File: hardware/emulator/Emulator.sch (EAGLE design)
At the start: 41 parts, among them T1 ZVP2106ASTZ, T2 2N5401, U1 DEV-16771_REDUCED_PINS, U2 OPA2277PA, U3 MCP4822-E/P, U4 LM6132BIN, U5 L7808ABV, U6 L7908CV

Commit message: Update info text
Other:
- note added: "Maximum Emulation Current: 4.095 / R_Range Example: 4.095 / 49.9 = 0.082064 A = 82.06 mA"
- note added: "V_OC = 2 * DAC_OC_VOLTAGE_EMULATION"
- note removed: "Maximum Emulation Current: 3.3 / R_Range Example: 3.3 / 49.9 = 0.0661322 A = 66.13 mA"
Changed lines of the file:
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@@
 <wire x1="144.78" y1="132.08" x2="96.52" y2="132.08" width="0.508" layer="97" style="longdash"/>
 <text x="109.22" y="134.62" size="1.778" layer="97">Solar Cell Model</text>
-<text x="73.66" y="157.48" size="1.778" layer="97">Maximum Emulation Current: 3.3 / R_Range
-Example: 3.3 / 49.9 = 0.0661322 A = 66.13 mA</text>
+<text x="73.66" y="157.48" size="1.778" layer="97">Maximum Emulation Current: 4.095 / R_Range
+Example: 4.095 / 49.9 = 0.082064 A = 82.06 mA</text>
 <text x="50.8" y="121.92" size="1.778" layer="97">I_OUT = DAC_SC / R_RANGE</text>
+<text x="149.86" y="73.66" size="1.778" layer="97" rot="R90">V_OC = 2 * DAC_OC_VOLTAGE_EMULATION</text>
 </plain>
 <instances>

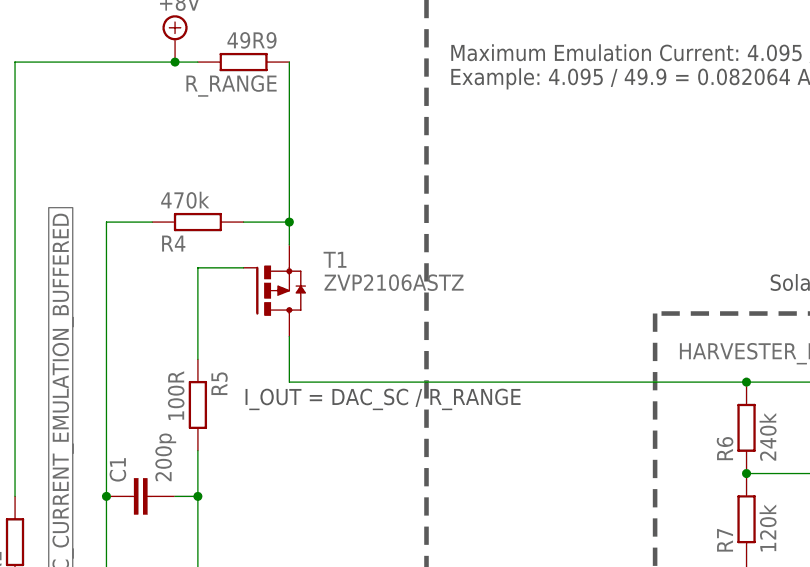
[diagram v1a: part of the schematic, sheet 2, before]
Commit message: Update the emulation MOSFET device
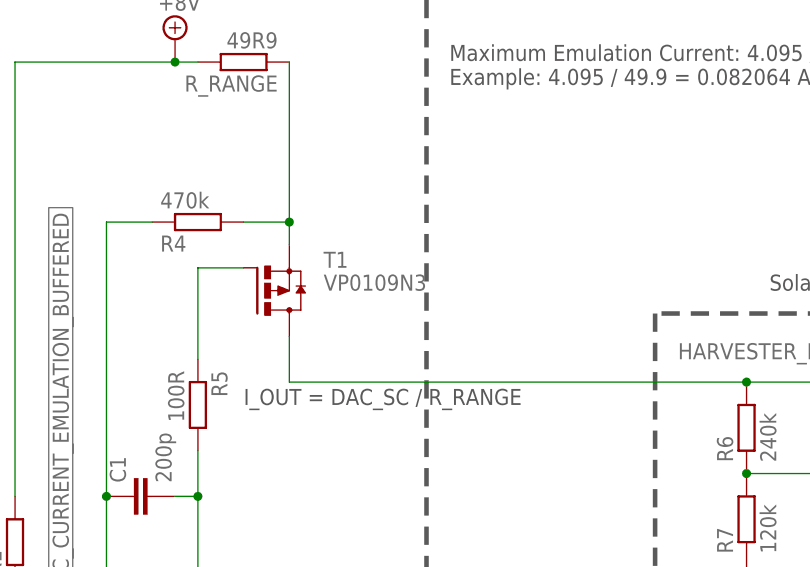
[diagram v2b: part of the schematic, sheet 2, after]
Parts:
- T1: value ZVP2106ASTZ -> VP0109N3; device ZVP2106A:ZVP2106ASTZ -> ZVP2106A:VP0109N3
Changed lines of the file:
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@@
 <part name="SUPPLY8" library="supply2" library_urn="urn:adsk.eagle:library:372" deviceset="GND" device=""/>
 <part name="SUPPLY18" library="supply2" library_urn="urn:adsk.eagle:library:372" deviceset="+8V" device=""/>
-<part name="T1" library="ZVP2106A" deviceset="ZVP2106ASTZ" device=""/>
+<part name="T1" library="ZVP2106A" deviceset="VP0109N3" device=""/>
 <part name="T2" library="transistor-neu-to92" deviceset="*-PNP-" device="TO92-EBC" package3d_urn="urn:adsk.eagle:package:28763/2" technology="2N5401" value="2N5401"/>
 <part name="R7" library="rcl" library_urn="urn:adsk.eagle:library:334" deviceset="R-EU_" device="0207/10" package3d_urn="urn:adsk.eagle:package:23491/2" value="120k"/>

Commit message: Update board version
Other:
- note added: "v0.3.11"
- note removed: "v0.2.3"
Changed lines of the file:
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@@
 <plain>
 <text x="215.9" y="20.32" size="2.54" layer="94">SOCRAETES Emulator</text>
-<text x="215.9" y="15.24" size="2.54" layer="94">v0.2.3</text>
+<text x="215.9" y="15.24" size="2.54" layer="94">v0.3.11</text>
 <text x="215.9" y="10.16" size="2.54" layer="94">Author: S.Mosavat</text>
 <text x="162.56" y="7.62" size="2.54" layer="94">University of Duisburg-Essen

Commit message: Add minor changes to the hardware
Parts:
- added T3: 2N5401, transistor-neu-to92:2N5401-PNP-TO92-EBC
- R1, R2: value 1k5 -> 1k
- R3, R4: value 470k -> 499k
- T2: value 2N5401 -> IRF9530PBF; device transistor-neu-to92:2N5401-PNP-TO92-EBC -> IRF9530PBF:IRF9530PBF
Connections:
- net GND: now also T3.C; no longer T2.C
- net HARVESTER_EMULATION: now also T2.D, T3.E; no longer T2.E
- net N$12: now also T3.B; no longer T2.B
- net N$5: now also T2.G
- net N$7: now also T2.S
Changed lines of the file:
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@@
 <part name="SUPPLY17" library="supply2" library_urn="urn:adsk.eagle:library:372" deviceset="-8V" device=""/>
 <part name="U2" library="OPA2277PA" deviceset="OPA2277PA" device=""/>
-<part name="R1" library="rcl" library_urn="urn:adsk.eagle:library:334" deviceset="R-EU_" device="0207/10" package3d_urn="urn:adsk.eagle:package:23491/2" value="1k5"/>
-<part name="R2" library="rcl" library_urn="urn:adsk.eagle:library:334" deviceset="R-EU_" device="0207/10" package3d_urn="urn:adsk.eagle:package:23491/2" value="1k5"/>
-<part name="R3" library="rcl" library_urn="urn:adsk.eagle:library:334" deviceset="R-EU_" device="0207/10" package3d_urn="urn:adsk.eagle:package:23491/2" value="470k"/>
-<part name="R4" library="rcl" library_urn="urn:adsk.eagle:library:334" deviceset="R-EU_" device="0207/10" package3d_urn="urn:adsk.eagle:package:23491/2" value="470k"/>
+<part name="R1" library="rcl" library_urn="urn:adsk.eagle:library:334" deviceset="R-EU_" device="0207/10" package3d_urn="urn:adsk.eagle:package:23491/2" value="1k"/>
+<part name="R2" library="rcl" library_urn="urn:adsk.eagle:library:334" deviceset="R-EU_" device="0207/10" package3d_urn="urn:adsk.eagle:package:23491/2" value="1k"/>
+<part name="R3" library="rcl" library_urn="urn:adsk.eagle:library:334" deviceset="R-EU_" device="0207/10" package3d_urn="urn:adsk.eagle:package:23491/2" value="499k"/>
+<part name="R4" library="rcl" library_urn="urn:adsk.eagle:library:334" deviceset="R-EU_" device="0207/10" package3d_urn="urn:adsk.eagle:package:23491/2" value="499k"/>
 <part name="R_RANGE" library="rcl" library_urn="urn:adsk.eagle:library:334" deviceset="R-EU_" device="0207/10" package3d_urn="urn:adsk.eagle:package:23491/2" value="49R9"/>
 <part name="R5" library="rcl" library_urn="urn:adsk.eagle:library:334" deviceset="R-EU_" device="0207/10" package3d_urn="urn:adsk.eagle:package:23491/2" value="100R"/>
@@
 <part name="SUPPLY18" library="supply2" library_urn="urn:adsk.eagle:library:372" deviceset="+8V" device=""/>
 <part name="T1" library="ZVP2106A" deviceset="VP0109N3" device=""/>
-<part name="T2" library="transistor-neu-to92" deviceset="*-PNP-" device="TO92-EBC" package3d_urn="urn:adsk.eagle:package:28763/2" technology="2N5401" value="2N5401"/>
+<part name="T3" library="transistor-neu-to92" deviceset="*-PNP-" device="TO92-EBC" package3d_urn="urn:adsk.eagle:package:28763/2" technology="2N5401" value="2N5401"/>
 <part name="R7" library="rcl" library_urn="urn:adsk.eagle:library:334" deviceset="R-EU_" device="0207/10" package3d_urn="urn:adsk.eagle:package:23491/2" value="120k"/>
 <part name="R6" library="rcl" library_urn="urn:adsk.eagle:library:334" deviceset="R-EU_" device="0207/10" package3d_urn="urn:adsk.eagle:package:23491/2" value="240k"/>
@@
 <part name="R11" library="rcl" library_urn="urn:adsk.eagle:library:334" deviceset="R-EU_" device="0207/10" package3d_urn="urn:adsk.eagle:package:23491/2" value="330R"/>
 <part name="ERROR" library="led" library_urn="urn:adsk.eagle:library:259" deviceset="LED" device="5MM" package3d_urn="urn:adsk.eagle:package:15799/2"/>
+<part name="T2" library="IRF9530PBF" deviceset="IRF9530PBF" device=""/>
 </parts>
 <sheets>
@@
 <description>Analog front-end</description>
 <plain>
-<wire x1="71.12" y1="170.18" x2="71.12" y2="40.64" width="0.508" layer="97" style="longdash"/>
-<wire x1="71.12" y1="40.64" x2="15.24" y2="40.64" width="0.508" layer="97" style="longdash"/>
+<wire x1="76.2" y1="170.18" x2="76.2" y2="40.64" width="0.508" layer="97" style="longdash"/>
+<wire x1="76.2" y1="40.64" x2="15.24" y2="40.64" width="0.508" layer="97" style="longdash"/>
 <wire x1="15.24" y1="40.64" x2="15.24" y2="170.18" width="0.508" layer="97" style="longdash"/>
-<wire x1="15.24" y1="170.18" x2="71.12" y2="170.18" width="0.508" layer="97" style="longdash"/>
+<wire x1="15.24" y1="170.18" x2="76.2" y2="170.18" width="0.508" layer="97" style="longdash"/>
 <text x="40.64" y="172.72" size="1.778" layer="97">Current Source</text>
 <wire x1="96.52" y1="132.08" x2="96.52" y2="17.78" width="0.508" layer="97" style="longdash"/>
@@
 <wire x1="144.78" y1="132.08" x2="96.52" y2="132.08" width="0.508" layer="97" style="longdash"/>
 <text x="109.22" y="134.62" size="1.778" layer="97">Solar Cell Model</text>
-<text x="73.66" y="157.48" size="1.778" layer="97">Maximum Emulation Current: 4.095 / R_Range
+<text x="78.74" y="157.48" size="1.778" layer="97">Maximum Emulation Current: 4.095 / R_Range
 Example: 4.095 / 49.9 = 0.082064 A = 82.06 mA</text>
 <text x="50.8" y="121.92" size="1.778" layer="97">I_OUT = DAC_SC / R_RANGE</text>
@@
 </instance>
 <instance part="T1" gate="A" x="53.34" y="134.62" smashed="yes">
-<attribute name="NAME" x="59.69" y="137.16" size="1.778" layer="95"/>
-<attribute name="VALUE" x="59.69" y="134.62" size="1.778" layer="96"/>
-</instance>
-<instance part="T2" gate="G$1" x="134.62" y="119.38" smashed="yes">
+<attribute name="NAME" x="48.768" y="133.35" size="1.778" layer="95"/>
+<attribute name="VALUE" x="59.182" y="130.048" size="1.778" layer="96" rot="R180"/>
+</instance>
+<instance part="T3" gate="G$1" x="134.62" y="119.38" smashed="yes">
 <attribute name="NAME" x="132.08" y="121.92" size="1.778" layer="95"/>
 <attribute name="VALUE" x="124.46" y="119.38" size="1.778" layer="96"/>
@@
 <attribute name="NAME" x="37.719" y="113.284" size="1.778" layer="95" rot="R90"/>
 <attribute name="VALUE" x="42.799" y="113.284" size="1.778" layer="96" rot="R90"/>
+</instance>
+<instance part="T2" gate="A" x="63.5" y="134.62" smashed="yes">
+<attribute name="NAME" x="62.992" y="131.953" size="1.778" layer="95" ratio="10" rot="SR0"/>
+<attribute name="VALUE" x="62.23" y="128.27" size="1.778" layer="96" ratio="10" rot="SR0"/>
 </instance>
 </instances>
@@
 </segment>
 <segment>
-<pinref part="T2" gate="G$1" pin="C"/>
+<pinref part="T3" gate="G$1" pin="C"/>
 <pinref part="SUPPLY19" gate="GND" pin="GND"/>
 <wire x1="137.16" y1="114.3" x2="137.16" y2="111.76" width="0.1524" layer="91"/>
@@
 <wire x1="50.8" y1="142.24" x2="55.88" y2="142.24" width="0.1524" layer="91"/>
 <junction x="55.88" y="142.24"/>
+<pinref part="T2" gate="A" pin="S"/>
+<wire x1="55.88" y1="142.24" x2="71.12" y2="142.24" width="0.1524" layer="91"/>
 </segment>
 </net>
@@
 <wire x1="45.72" y1="127" x2="45.72" y2="137.16" width="0.1524" layer="91"/>
 <wire x1="45.72" y1="137.16" x2="50.8" y2="137.16" width="0.1524" layer="91"/>
+<wire x1="50.8" y1="137.16" x2="50.8" y2="139.7" width="0.1524" layer="91"/>
+<junction x="50.8" y="137.16"/>
+<wire x1="50.8" y1="139.7" x2="63.5" y2="139.7" width="0.1524" layer="91"/>
+<pinref part="T2" gate="A" pin="G"/>
+<wire x1="63.5" y1="139.7" x2="63.5" y2="134.62" width="0.1524" layer="91"/>
 </segment>
 </net>
@@
 <pinref part="T1" gate="A" pin="D"/>
 <wire x1="55.88" y1="129.54" x2="55.88" y2="124.46" width="0.1524" layer="91"/>
-<wire x1="55.88" y1="124.46" x2="106.68" y2="124.46" width="0.1524" layer="91"/>
-<pinref part="T2" gate="G$1" pin="E"/>
+<pinref part="T3" gate="G$1" pin="E"/>
 <pinref part="R6" gate="G$1" pin="2"/>
+<wire x1="55.88" y1="124.46" x2="71.12" y2="124.46" width="0.1524" layer="91"/>
+<wire x1="71.12" y1="124.46" x2="106.68" y2="124.46" width="0.1524" layer="91"/>
 <wire x1="106.68" y1="124.46" x2="116.84" y2="124.46" width="0.1524" layer="91"/>
 <junction x="106.68" y="124.46"/>
@@
 <junction x="116.84" y="124.46"/>
 <label x="99.06" y="127" size="1.778" layer="95"/>
+<pinref part="T2" gate="A" pin="D"/>
+<wire x1="71.12" y1="127" x2="71.12" y2="124.46" width="0.1524" layer="91"/>
+<junction x="71.12" y="124.46"/>
 </segment>
 </net>
@@
 <segment>
 <pinref part="R8" gate="G$1" pin="2"/>
-<pinref part="T2" gate="G$1" pin="B"/>
+<pinref part="T3" gate="G$1" pin="B"/>
 <wire x1="127" y1="111.76" x2="127" y2="119.38" width="0.1524" layer="91"/>
 <wire x1="127" y1="119.38" x2="132.08" y2="119.38" width="0.1524" layer="91"/>

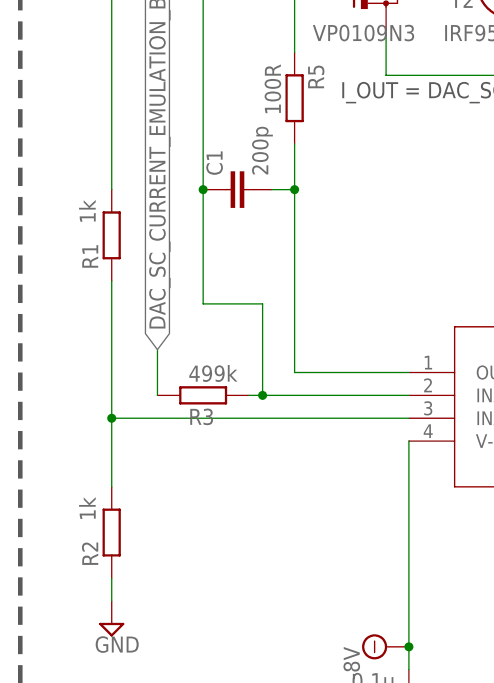
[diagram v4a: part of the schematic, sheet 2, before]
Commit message: Update resistor value
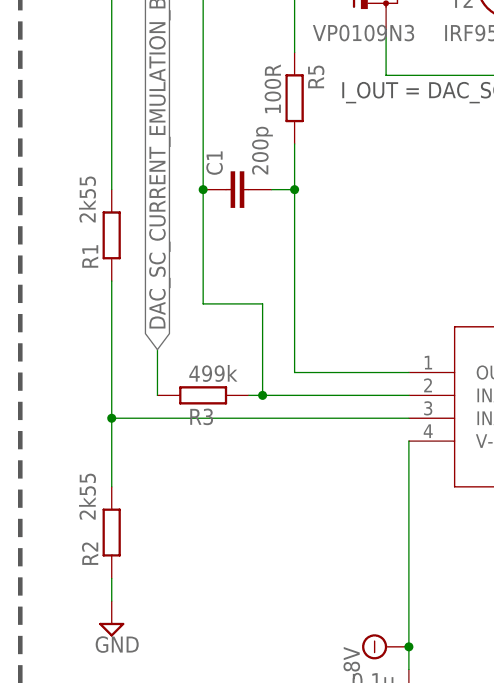
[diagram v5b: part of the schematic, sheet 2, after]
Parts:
- R1, R2: value 1k -> 2k55
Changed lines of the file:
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@@
 <part name="SUPPLY17" library="supply2" library_urn="urn:adsk.eagle:library:372" deviceset="-8V" device=""/>
 <part name="U2" library="OPA2277PA" deviceset="OPA2277PA" device=""/>
-<part name="R1" library="rcl" library_urn="urn:adsk.eagle:library:334" deviceset="R-EU_" device="0207/10" package3d_urn="urn:adsk.eagle:package:23491/2" value="1k"/>
-<part name="R2" library="rcl" library_urn="urn:adsk.eagle:library:334" deviceset="R-EU_" device="0207/10" package3d_urn="urn:adsk.eagle:package:23491/2" value="1k"/>
+<part name="R1" library="rcl" library_urn="urn:adsk.eagle:library:334" deviceset="R-EU_" device="0207/10" package3d_urn="urn:adsk.eagle:package:23491/2" value="2k55"/>
+<part name="R2" library="rcl" library_urn="urn:adsk.eagle:library:334" deviceset="R-EU_" device="0207/10" package3d_urn="urn:adsk.eagle:package:23491/2" value="2k55"/>
 <part name="R3" library="rcl" library_urn="urn:adsk.eagle:library:334" deviceset="R-EU_" device="0207/10" package3d_urn="urn:adsk.eagle:package:23491/2" value="499k"/>
 <part name="R4" library="rcl" library_urn="urn:adsk.eagle:library:334" deviceset="R-EU_" device="0207/10" package3d_urn="urn:adsk.eagle:package:23491/2" value="499k"/>
